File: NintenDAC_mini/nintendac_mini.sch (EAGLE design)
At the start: 30 parts, among them IC1 STM32F10XCXT6, IC3 24C64ST, X1 USB-MICROB

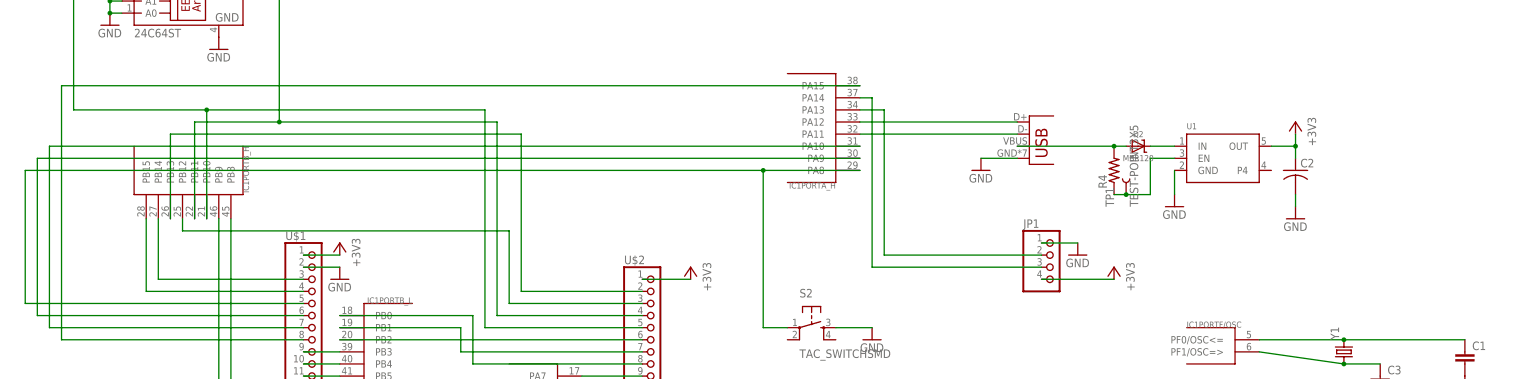
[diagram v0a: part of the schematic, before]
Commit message: updated power control on mini
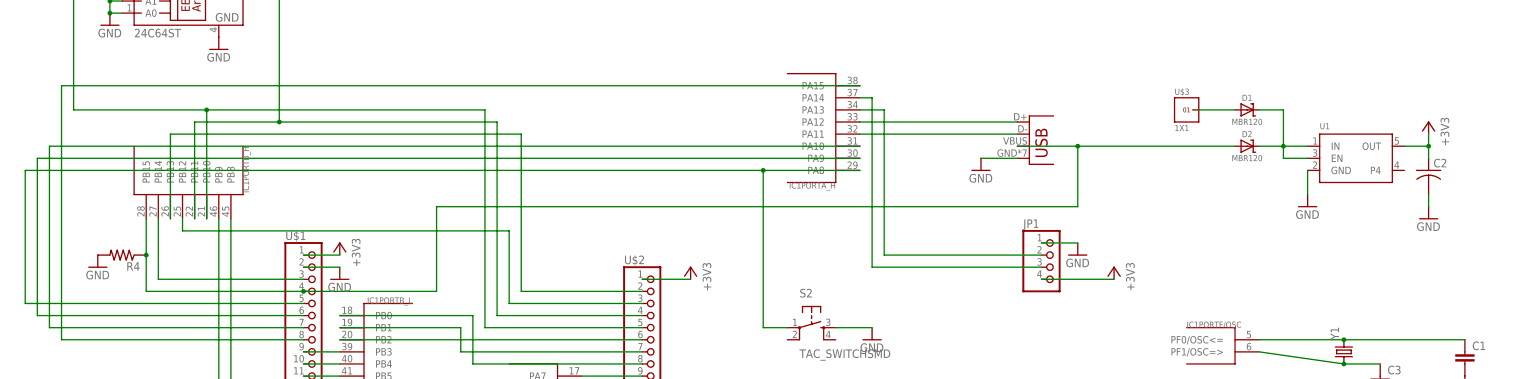
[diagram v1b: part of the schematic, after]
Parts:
- removed TP1: TEST-POINT3X5, SparkFun-Passives:TEST-POINT3X5
- added D1: MBR120, microbuilder:DIODE-SCHOTTKYSOD-123
- added U$3: 1X1, headers(2mm):1X1
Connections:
- removed net N$2: D2.A, R4.2, X1.VBUS
- net GND: now also R4.2
- net N$31: now also D1.C, U1.EN
- net N$36: now also D1.A, U$3.1; no longer R4.1, TP1.1, U1.EN
- net N$45: now also D2.A, R4.1, X1.VBUS
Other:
- moved on the sheet: C2, D2, R4, U1
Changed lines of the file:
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@@
 <part name="D2" library="microbuilder" deviceset="DIODE-SCHOTTKY" device="SOD-123" value="MBR120"/>
 <part name="GND6" library="backplane" deviceset="GND" device=""/>
+<part name="D1" library="microbuilder" deviceset="DIODE-SCHOTTKY" device="SOD-123" value="MBR120"/>
+<part name="U$3" library="headers(2mm)" deviceset="1X1" device=""/>
 <part name="R4" library="SparkFun-Passives" deviceset="RESISTOR" device="0805-RES"/>
-<part name="TP1" library="SparkFun-Passives" deviceset="TEST-POINT" device="3X5"/>
+<part name="GND9" library="backplane" deviceset="GND" device=""/>
 </parts>
 <sheets>
@@
 <instance part="+3V1" gate="G$1" x="-93.98" y="162.56"/>
 <instance part="C1" gate="G$1" x="190.5" y="-83.82"/>
-<instance part="C2" gate="G$1" x="154.94" y="-43.18"/>
+<instance part="C2" gate="G$1" x="182.88" y="-43.18"/>
 <instance part="Y1" gate="G$1" x="165.1" y="-81.28" rot="R90"/>
 <instance part="X1" gate="G$1" x="99.06" y="-40.64"/>
@@
 <instance part="GND3" gate="1" x="-93.98" y="111.76"/>
 <instance part="GND5" gate="1" x="88.9" y="-43.18"/>
-<instance part="+3V3" gate="G$1" x="154.94" y="-33.02" rot="MR0"/>
+<instance part="+3V3" gate="G$1" x="182.88" y="-33.02" rot="MR0"/>
 <instance part="S1" gate="G$1" x="165.1" y="-106.68"/>
 <instance part="C3" gate="G$1" x="172.72" y="-88.9"/>
 <instance part="GND7" gate="1" x="172.72" y="-93.98"/>
 <instance part="GND8" gate="1" x="190.5" y="-88.9"/>
-<instance part="GND10" gate="1" x="154.94" y="-53.34"/>
+<instance part="GND10" gate="1" x="182.88" y="-53.34"/>
 <instance part="C6" gate="G$1" x="25.4" y="101.6"/>
 <instance part="C7" gate="G$1" x="38.1" y="101.6"/>
@@
 <instance part="S2" gate="S" x="53.34" y="-76.2"/>
 <instance part="GND17" gate="1" x="66.04" y="-78.74"/>
-<instance part="U1" gate="G$1" x="139.7" y="-40.64"/>
-<instance part="D2" gate="G$1" x="121.92" y="-38.1"/>
-<instance part="GND6" gate="1" x="129.54" y="-50.8"/>
-<instance part="R4" gate="G$1" x="116.84" y="-43.18" rot="R90"/>
-<instance part="TP1" gate="G$1" x="119.38" y="-48.26" rot="R90"/>
+<instance part="U1" gate="G$1" x="167.64" y="-40.64"/>
+<instance part="D2" gate="G$1" x="144.78" y="-38.1"/>
+<instance part="GND6" gate="1" x="157.48" y="-50.8"/>
+<instance part="D1" gate="G$1" x="144.78" y="-30.48"/>
+<instance part="U$3" gate="G$1" x="132.08" y="-30.48"/>
+<instance part="R4" gate="G$1" x="-91.44" y="-60.96" rot="R180"/>
+<instance part="GND9" gate="1" x="-96.52" y="-63.5"/>
 </instances>
 <busses>
@@
 <pinref part="C2" gate="G$1" pin="2"/>
 <pinref part="GND10" gate="1" pin="GND"/>
-<wire x1="154.94" y1="-50.8" x2="154.94" y2="-48.26" width="0.1524" layer="91"/>
+<wire x1="182.88" y1="-50.8" x2="182.88" y2="-48.26" width="0.1524" layer="91"/>
 </segment>
 <segment>
@@
 <pinref part="U1" gate="G$1" pin="GND"/>
 <pinref part="GND6" gate="1" pin="GND"/>
-<wire x1="129.54" y1="-43.18" x2="129.54" y2="-48.26" width="0.1524" layer="91"/>
+<wire x1="157.48" y1="-43.18" x2="157.48" y2="-48.26" width="0.1524" layer="91"/>
+</segment>
+<segment>
+<pinref part="R4" gate="G$1" pin="2"/>
+<pinref part="GND9" gate="1" pin="GND"/>
 </segment>
 </net>
@@
 <pinref part="C2" gate="G$1" pin="1"/>
 <pinref part="+3V3" gate="G$1" pin="+3V3"/>
-<wire x1="154.94" y1="-40.64" x2="154.94" y2="-38.1" width="0.1524" layer="91"/>
+<wire x1="182.88" y1="-40.64" x2="182.88" y2="-38.1" width="0.1524" layer="91"/>
 <pinref part="U1" gate="G$1" pin="OUT"/>
-<wire x1="154.94" y1="-38.1" x2="154.94" y2="-35.56" width="0.1524" layer="91"/>
-<wire x1="149.86" y1="-38.1" x2="154.94" y2="-38.1" width="0.1524" layer="91"/>
-<junction x="154.94" y="-38.1"/>
+<wire x1="182.88" y1="-38.1" x2="182.88" y2="-35.56" width="0.1524" layer="91"/>
+<wire x1="177.8" y1="-38.1" x2="182.88" y2="-38.1" width="0.1524" layer="91"/>
+<junction x="182.88" y="-38.1"/>
 </segment>
 <segment>
@@
 <pinref part="IC1" gate="PORTB_H" pin="PB15"/>
 <pinref part="U$1" gate="G$1" pin="4"/>
-<wire x1="-86.36" y1="-53.34" x2="-86.36" y2="-68.58" width="0.1524" layer="91"/>
+<wire x1="-86.36" y1="-53.34" x2="-86.36" y2="-60.96" width="0.1524" layer="91"/>
+<wire x1="-86.36" y1="-60.96" x2="-86.36" y2="-68.58" width="0.1524" layer="91"/>
 <wire x1="-86.36" y1="-68.58" x2="-53.34" y2="-68.58" width="0.1524" layer="91"/>
-</segment>
-</net>
-<net name="N$2" class="0">
-<segment>
+<pinref part="R4" gate="G$1" pin="1"/>
+<junction x="-86.36" y="-60.96"/>
+<wire x1="-53.34" y1="-68.58" x2="-25.4" y2="-68.58" width="0.1524" layer="91"/>
+<wire x1="-25.4" y1="-68.58" x2="-25.4" y2="-50.8" width="0.1524" layer="91"/>
+<junction x="-53.34" y="-68.58"/>
+<pinref part="D2" gate="G$1" pin="A"/>
 <pinref part="X1" gate="G$1" pin="VBUS"/>
-<wire x1="96.52" y1="-38.1" x2="116.84" y2="-38.1" width="0.1524" layer="91"/>
-<pinref part="D2" gate="G$1" pin="A"/>
-<pinref part="R4" gate="G$1" pin="2"/>
-<wire x1="116.84" y1="-38.1" x2="119.38" y2="-38.1" width="0.1524" layer="91"/>
-<junction x="116.84" y="-38.1"/>
-</segment>
-</net>
-<net name="N$36" class="0">
-<segment>
-<pinref part="R4" gate="G$1" pin="1"/>
-<wire x1="116.84" y1="-48.26" x2="119.38" y2="-48.26" width="0.1524" layer="91"/>
-<wire x1="119.38" y1="-48.26" x2="124.46" y2="-48.26" width="0.1524" layer="91"/>
-<wire x1="124.46" y1="-48.26" x2="124.46" y2="-40.64" width="0.1524" layer="91"/>
-<pinref part="U1" gate="G$1" pin="EN"/>
-<wire x1="124.46" y1="-40.64" x2="129.54" y2="-40.64" width="0.1524" layer="91"/>
-<pinref part="TP1" gate="G$1" pin="1"/>
-<junction x="119.38" y="-48.26"/>
+<wire x1="96.52" y1="-38.1" x2="109.22" y2="-38.1" width="0.1524" layer="91"/>
+<wire x1="109.22" y1="-38.1" x2="142.24" y2="-38.1" width="0.1524" layer="91"/>
+<wire x1="-25.4" y1="-50.8" x2="109.22" y2="-50.8" width="0.1524" layer="91"/>
+<wire x1="109.22" y1="-50.8" x2="109.22" y2="-38.1" width="0.1524" layer="91"/>
+<junction x="109.22" y="-38.1"/>
 </segment>
 </net>
@@
 <pinref part="U1" gate="G$1" pin="IN"/>
 <pinref part="D2" gate="G$1" pin="C"/>
-<wire x1="124.46" y1="-38.1" x2="129.54" y2="-38.1" width="0.1524" layer="91"/>
-</segment>
-</net>
+<wire x1="147.32" y1="-38.1" x2="152.4" y2="-38.1" width="0.1524" layer="91"/>
+<pinref part="D1" gate="G$1" pin="C"/>
+<wire x1="152.4" y1="-38.1" x2="157.48" y2="-38.1" width="0.1524" layer="91"/>
+<wire x1="147.32" y1="-30.48" x2="152.4" y2="-30.48" width="0.1524" layer="91"/>
+<wire x1="152.4" y1="-30.48" x2="152.4" y2="-38.1" width="0.1524" layer="91"/>
+<junction x="152.4" y="-38.1"/>
+<pinref part="U1" gate="G$1" pin="EN"/>
+<wire x1="157.48" y1="-40.64" x2="152.4" y2="-40.64" width="0.1524" layer="91"/>
+<wire x1="152.4" y1="-40.64" x2="152.4" y2="-38.1" width="0.1524" layer="91"/>
+</segment>
+</net>
+<net name="N$36" class="0">
+<segment>
+<pinref part="D1" gate="G$1" pin="A"/>
+<pinref part="U$3" gate="G$1" pin="1"/>
+<wire x1="134.62" y1="-30.48" x2="142.24" y2="-30.48" width="0.1524" layer="91"/>
+</segment>
+</net>

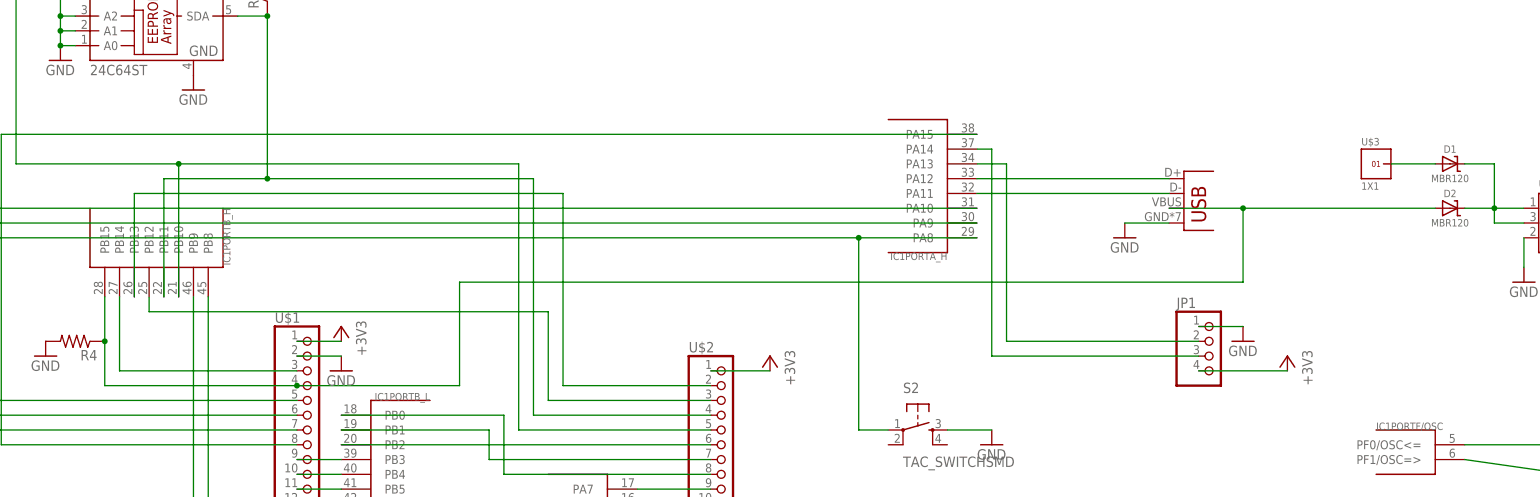
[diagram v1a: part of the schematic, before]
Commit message: removed wkup from headers
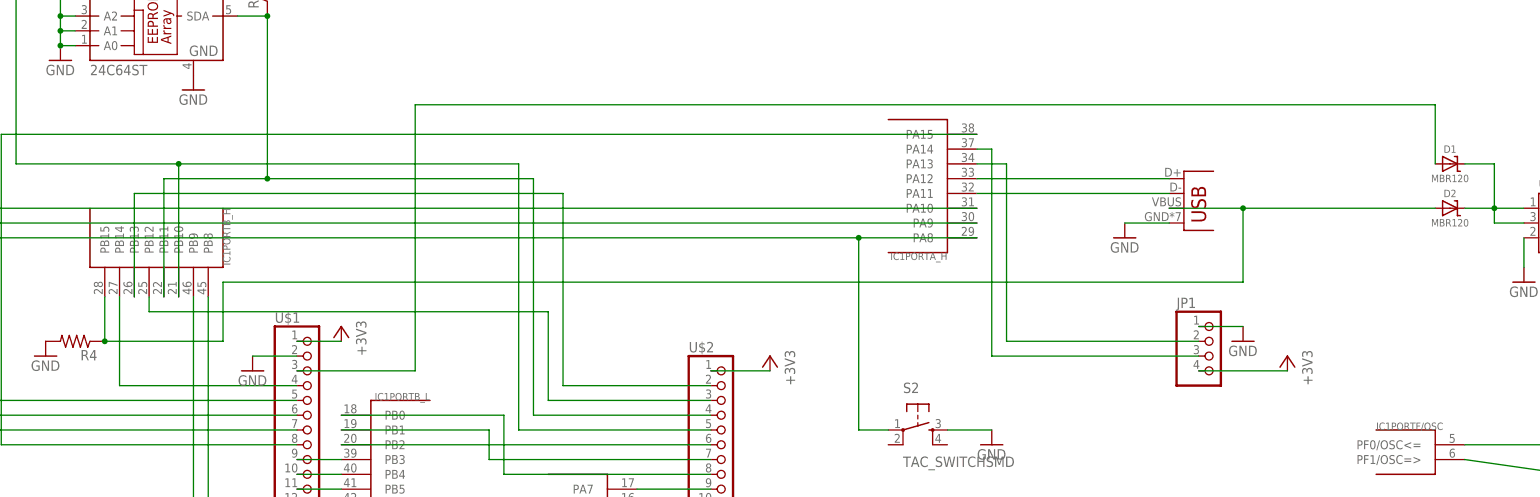
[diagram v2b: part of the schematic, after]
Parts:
- removed U$3: 1X1, headers(2mm):1X1
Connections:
- removed net N$36: D1.A, U$3.1
- new net N$2: D1.A, U$1.3
- net N$44: now also U$1.4; no longer U$1.3
- net N$45: no longer U$1.4
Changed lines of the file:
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@@
 <part name="GND6" library="backplane" deviceset="GND" device=""/>
 <part name="D1" library="microbuilder" deviceset="DIODE-SCHOTTKY" device="SOD-123" value="MBR120"/>
-<part name="U$3" library="headers(2mm)" deviceset="1X1" device=""/>
 <part name="R4" library="SparkFun-Passives" deviceset="RESISTOR" device="0805-RES"/>
 <part name="GND9" library="backplane" deviceset="GND" device=""/>
@@
 <instance part="+3V8" gate="G$1" x="27.94" y="-63.5" rot="MR0"/>
 <instance part="+3V9" gate="G$1" x="-45.72" y="-58.42" rot="MR0"/>
-<instance part="GND16" gate="1" x="-45.72" y="-66.04"/>
+<instance part="GND16" gate="1" x="-60.96" y="-66.04"/>
 <instance part="S2" gate="S" x="53.34" y="-76.2"/>
 <instance part="GND17" gate="1" x="66.04" y="-78.74"/>
@@
 <instance part="GND6" gate="1" x="157.48" y="-50.8"/>
 <instance part="D1" gate="G$1" x="144.78" y="-30.48"/>
-<instance part="U$3" gate="G$1" x="132.08" y="-30.48"/>
 <instance part="R4" gate="G$1" x="-91.44" y="-60.96" rot="R180"/>
 <instance part="GND9" gate="1" x="-96.52" y="-63.5"/>
@@
 <pinref part="U$1" gate="G$1" pin="2"/>
 <pinref part="GND16" gate="1" pin="GND"/>
-<wire x1="-53.34" y1="-63.5" x2="-45.72" y2="-63.5" width="0.1524" layer="91"/>
+<wire x1="-53.34" y1="-63.5" x2="-60.96" y2="-63.5" width="0.1524" layer="91"/>
 </segment>
 <segment>
@@
 <segment>
 <pinref part="IC1" gate="PORTB_H" pin="PB14"/>
-<pinref part="U$1" gate="G$1" pin="3"/>
-<wire x1="-83.82" y1="-53.34" x2="-83.82" y2="-66.04" width="0.1524" layer="91"/>
-<wire x1="-83.82" y1="-66.04" x2="-53.34" y2="-66.04" width="0.1524" layer="91"/>
+<wire x1="-83.82" y1="-53.34" x2="-83.82" y2="-68.58" width="0.1524" layer="91"/>
+<pinref part="U$1" gate="G$1" pin="4"/>
+<wire x1="-83.82" y1="-68.58" x2="-53.34" y2="-68.58" width="0.1524" layer="91"/>
 </segment>
 </net>
 <net name="N$45" class="0">
 <segment>
-<pinref part="IC1" gate="PORTB_H" pin="PB15"/>
-<pinref part="U$1" gate="G$1" pin="4"/>
-<wire x1="-86.36" y1="-53.34" x2="-86.36" y2="-60.96" width="0.1524" layer="91"/>
-<wire x1="-86.36" y1="-60.96" x2="-86.36" y2="-68.58" width="0.1524" layer="91"/>
-<wire x1="-86.36" y1="-68.58" x2="-53.34" y2="-68.58" width="0.1524" layer="91"/>
-<pinref part="R4" gate="G$1" pin="1"/>
-<junction x="-86.36" y="-60.96"/>
-<wire x1="-53.34" y1="-68.58" x2="-25.4" y2="-68.58" width="0.1524" layer="91"/>
-<wire x1="-25.4" y1="-68.58" x2="-25.4" y2="-50.8" width="0.1524" layer="91"/>
-<junction x="-53.34" y="-68.58"/>
 <pinref part="D2" gate="G$1" pin="A"/>
 <pinref part="X1" gate="G$1" pin="VBUS"/>
 <wire x1="96.52" y1="-38.1" x2="109.22" y2="-38.1" width="0.1524" layer="91"/>
 <wire x1="109.22" y1="-38.1" x2="142.24" y2="-38.1" width="0.1524" layer="91"/>
-<wire x1="-25.4" y1="-50.8" x2="109.22" y2="-50.8" width="0.1524" layer="91"/>
+<wire x1="-66.04" y1="-50.8" x2="109.22" y2="-50.8" width="0.1524" layer="91"/>
 <wire x1="109.22" y1="-50.8" x2="109.22" y2="-38.1" width="0.1524" layer="91"/>
 <junction x="109.22" y="-38.1"/>
+<wire x1="-66.04" y1="-50.8" x2="-66.04" y2="-60.96" width="0.1524" layer="91"/>
+<pinref part="R4" gate="G$1" pin="1"/>
+<pinref part="IC1" gate="PORTB_H" pin="PB15"/>
+<wire x1="-86.36" y1="-53.34" x2="-86.36" y2="-60.96" width="0.1524" layer="91"/>
+<wire x1="-66.04" y1="-60.96" x2="-86.36" y2="-60.96" width="0.1524" layer="91"/>
+<junction x="-86.36" y="-60.96"/>
 </segment>
 </net>
@@
 </segment>
 </net>
-<net name="N$36" class="0">
+<net name="N$2" class="0">
 <segment>
 <pinref part="D1" gate="G$1" pin="A"/>
-<pinref part="U$3" gate="G$1" pin="1"/>
-<wire x1="134.62" y1="-30.48" x2="142.24" y2="-30.48" width="0.1524" layer="91"/>
-</segment>
-</net>
+<wire x1="142.24" y1="-30.48" x2="142.24" y2="-20.32" width="0.1524" layer="91"/>
+<wire x1="142.24" y1="-20.32" x2="-33.02" y2="-20.32" width="0.1524" layer="91"/>
+<pinref part="U$1" gate="G$1" pin="3"/>
+<wire x1="-33.02" y1="-20.32" x2="-33.02" y2="-66.04" width="0.1524" layer="91"/>
+<wire x1="-33.02" y1="-66.04" x2="-53.34" y2="-66.04" width="0.1524" layer="91"/>
+</segment>
+</net>
